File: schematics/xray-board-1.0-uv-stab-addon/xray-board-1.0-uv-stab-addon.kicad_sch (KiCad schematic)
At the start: 13 parts, among them J1 Conn_01x01_Pin, J2 Conn_01x01_Pin, J3 Conn_01x01_Pin, J4 Conn_01x01_Pin, Q11 IRLML0030, Q9 IRLML5203, U1 AMS1117-3.3

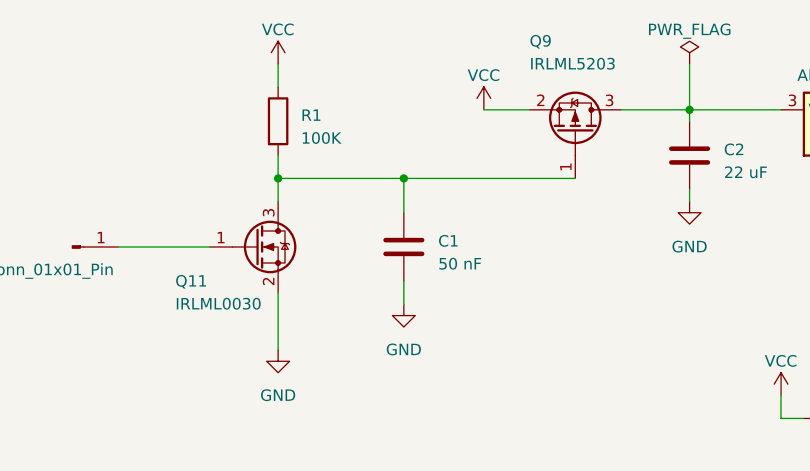
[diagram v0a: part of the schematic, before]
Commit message: changes in 3D model
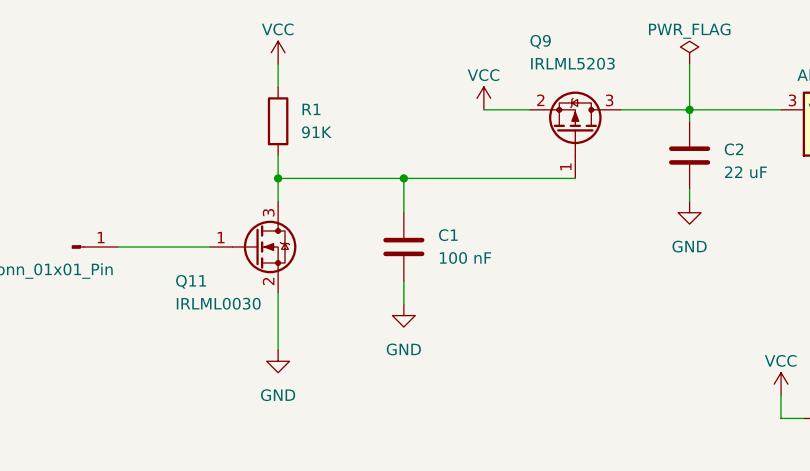
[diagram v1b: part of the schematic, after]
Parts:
- C1: value 50 nF -> 100 nF
- R1: value 100K -> 91K
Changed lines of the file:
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@@
   (symbol (lib_id "Device:R") (at 109.22 78.74 0) (unit 1)
     (in_bom yes) (on_board yes) (dnp no) (fields_autoplaced)
-    (property "Reference" "R1" (at 111.76 78.105 0)
-      (effects (font (size 1.27 1.27)) (justify left))
-    )
-    (property "Value" "100K" (at 111.76 80.645 0)
+    (property "Reference" "R1" (at 111.76 77.47 0)
+      (effects (font (size 1.27 1.27)) (justify left))
+    )
+    (property "Value" "91K" (at 111.76 80.01 0)
       (effects (font (size 1.27 1.27)) (justify left))
     )
@@
   (symbol (lib_id "Device:C") (at 123.19 92.71 0) (unit 1)
     (in_bom yes) (on_board yes) (dnp no) (fields_autoplaced)
-    (property "Reference" "C1" (at 127 92.075 0)
-      (effects (font (size 1.27 1.27)) (justify left))
-    )
-    (property "Value" "50 nF" (at 127 94.615 0)
-      (effects (font (size 1.27 1.27)) (justify left))
-    )
+    (property "Reference" "C1" (at 127 91.44 0)
+      (effects (font (size 1.27 1.27)) (justify left))
+    )
+    (property "Value" "100 nF" (at 127 93.98 0)
+      (effects (font (size 1.27 1.27)) (justify left))
+    )
